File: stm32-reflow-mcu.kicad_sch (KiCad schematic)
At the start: 18 parts, among them J1 TC2030, J2 Conn_01x04_Male, J3 Conn_01x03_Male, J4 Screw_Terminal_01x02, J5 Screw_Terminal_01x02, U1 STM32F051R4Tx, U2 MAX31855KASA, U3 MAX31855KASA

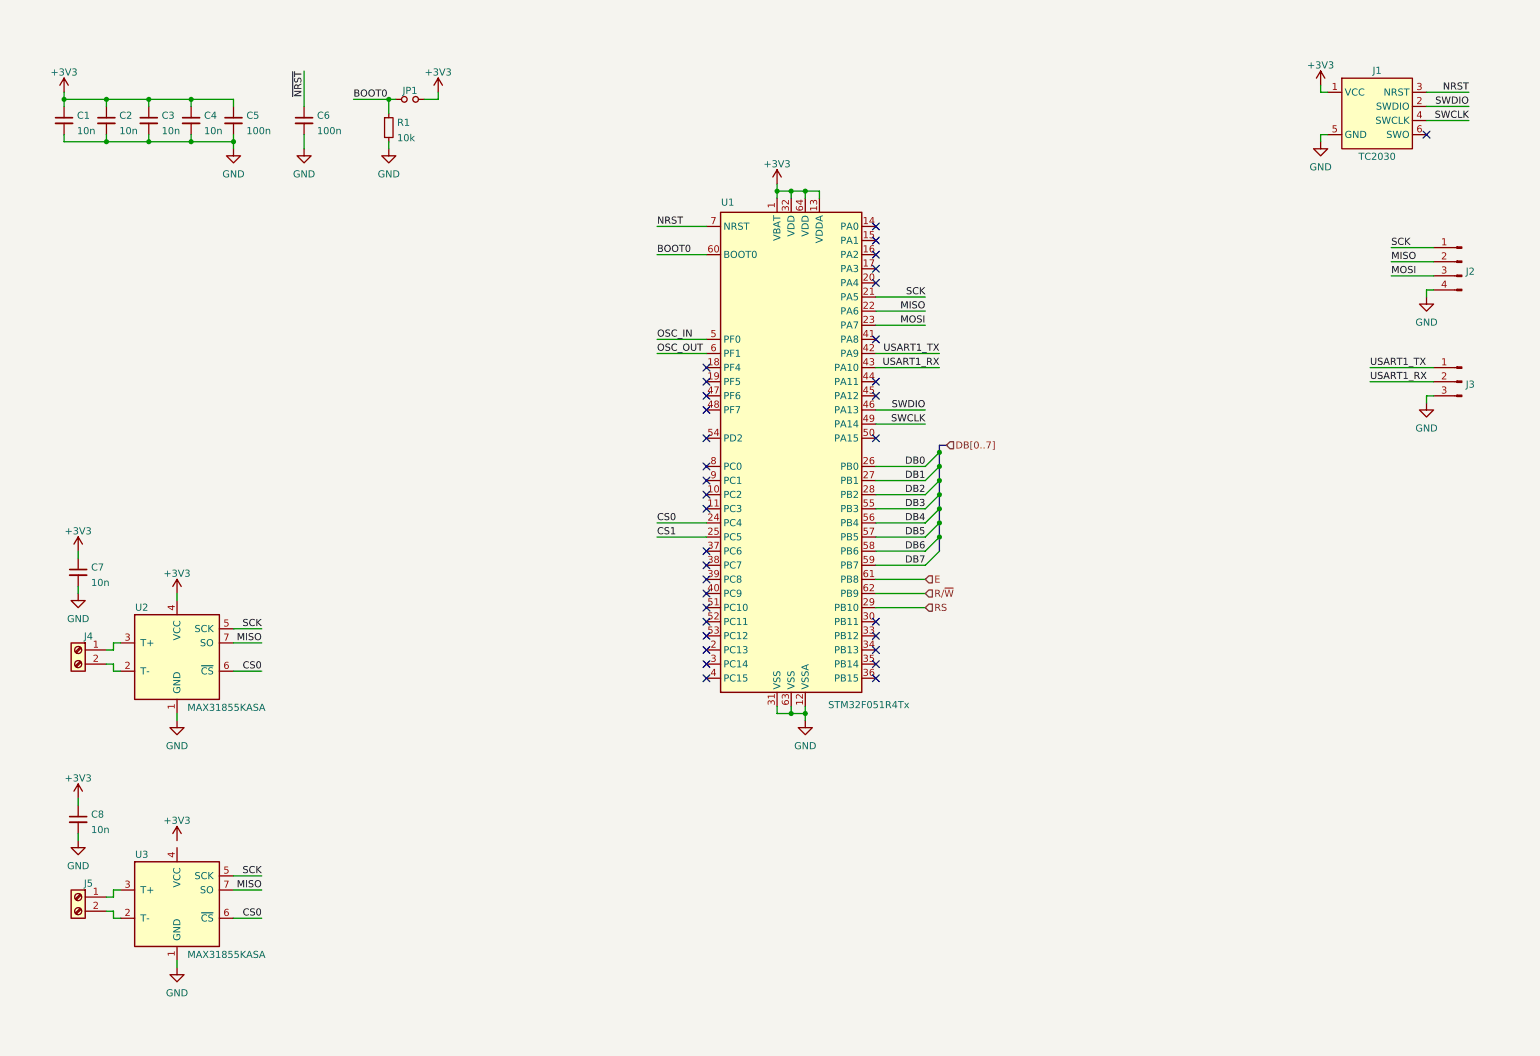
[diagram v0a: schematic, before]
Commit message: initial routing, added power supply source
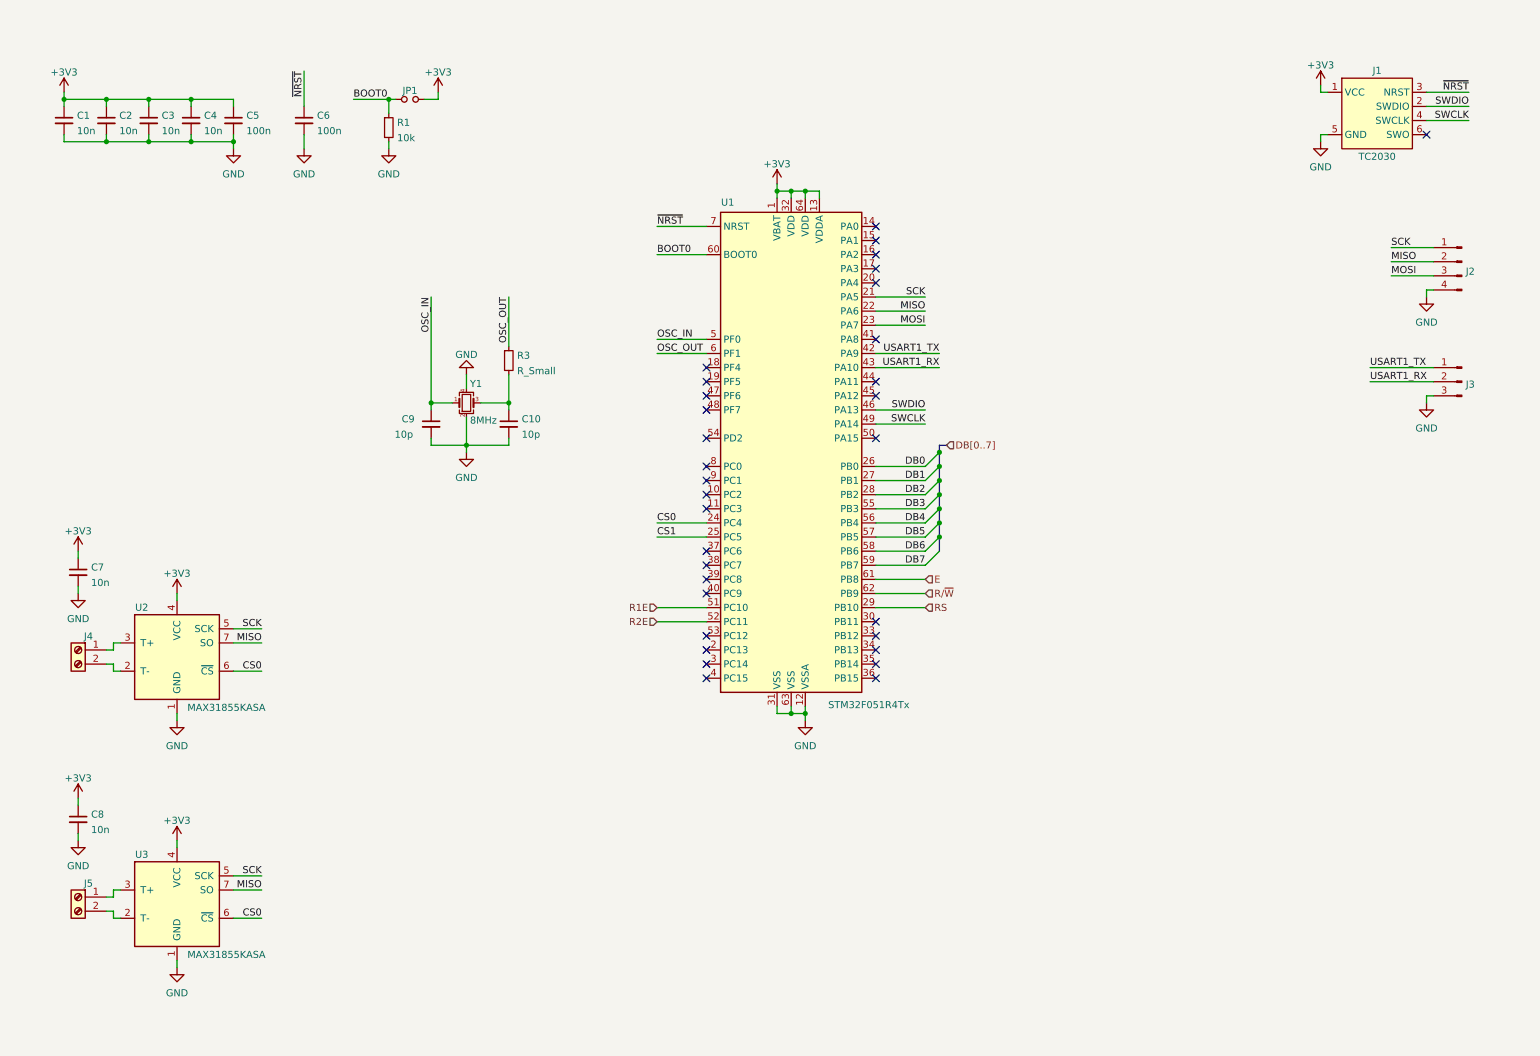
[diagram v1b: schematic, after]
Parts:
- added C10, C9: 10p, Capacitor_SMD:C_0603_1608Metric, symbol Device:C_Small
- added R3: R_Small, Resistor_SMD:R_0603_1608Metric, symbol Device:R_Small
- added Y1: 8MHz, Crystal:Crystal_SMD_5032-4Pin_5.0x3.2mm, symbol Device:Crystal_GND24_Small
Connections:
- net NRST is gone; now on net ~{NRST}: J1.3 (NRST), U1.7 (NRST)
- net +3V3: now also U3.4 (VCC)
- net GND: now also C10.2, C9.2, Y1.2, Y1.4
- net OSC_IN: now also C9.1, Y1.1
- net OSC_OUT: now also R3.1
- net R1E: now reaches U1.51 (PC10)
- net R2E: now reaches U1.52 (PC11)
- new net: C10.1, R3.2, Y1.3
- no-connect marks 34 -> 32
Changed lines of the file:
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@@
   (junction (at 52.07 35.56) (diameter 0) (color 0 0 0 0))
   (junction (at 80.01 27.94) (diameter 0) (color 0 0 0 0))
+  (junction (at 87.63 82.55) (diameter 0) (color 0 0 0 0))
+  (junction (at 93.98 90.17) (diameter 0) (color 0 0 0 0))
+  (junction (at 101.6 82.55) (diameter 0) (color 0 0 0 0))
   (junction (at 149.86 44.45) (diameter 0) (color 0 0 0 0))
   (junction (at 152.4 44.45) (diameter 0) (color 0 0 0 0))
@@
   (no_connect (at 137.16 114.3))
   (no_connect (at 137.16 116.84))
-  (no_connect (at 137.16 119.38))
-  (no_connect (at 137.16 121.92))
   (no_connect (at 137.16 124.46))
   (no_connect (at 137.16 127))
@@
     (stroke (width 0) (type default) (color 0 0 0 0))
   )
+  (wire (pts (xy 41.91 161.29) (xy 41.91 162.56))
+    (stroke (width 0) (type default) (color 0 0 0 0))
+  )
   (wire (pts (xy 41.91 182.88) (xy 41.91 184.15))
     (stroke (width 0) (type default) (color 0 0 0 0))
@@
     (stroke (width 0) (type default) (color 0 0 0 0))
   )
+  (wire (pts (xy 87.63 63.5) (xy 87.63 82.55))
+    (stroke (width 0) (type default) (color 0 0 0 0))
+  )
+  (wire (pts (xy 87.63 82.55) (xy 91.44 82.55))
+    (stroke (width 0) (type default) (color 0 0 0 0))
+  )
+  (wire (pts (xy 87.63 83.82) (xy 87.63 82.55))
+    (stroke (width 0) (type default) (color 0 0 0 0))
+  )
+  (wire (pts (xy 87.63 88.9) (xy 87.63 90.17))
+    (stroke (width 0) (type default) (color 0 0 0 0))
+  )
+  (wire (pts (xy 87.63 90.17) (xy 93.98 90.17))
+    (stroke (width 0) (type default) (color 0 0 0 0))
+  )
   (wire (pts (xy 88.9 27.94) (xy 88.9 26.67))
     (stroke (width 0) (type default) (color 0 0 0 0))
   )
+  (wire (pts (xy 93.98 77.47) (xy 93.98 80.01))
+    (stroke (width 0) (type default) (color 0 0 0 0))
+  )
+  (wire (pts (xy 93.98 85.09) (xy 93.98 90.17))
+    (stroke (width 0) (type default) (color 0 0 0 0))
+  )
+  (wire (pts (xy 93.98 90.17) (xy 93.98 91.44))
+    (stroke (width 0) (type default) (color 0 0 0 0))
+  )
+  (wire (pts (xy 93.98 90.17) (xy 101.6 90.17))
+    (stroke (width 0) (type default) (color 0 0 0 0))
+  )
+  (wire (pts (xy 96.52 82.55) (xy 101.6 82.55))
+    (stroke (width 0) (type default) (color 0 0 0 0))
+  )
+  (wire (pts (xy 101.6 63.5) (xy 101.6 72.39))
+    (stroke (width 0) (type default) (color 0 0 0 0))
+  )
+  (wire (pts (xy 101.6 77.47) (xy 101.6 82.55))
+    (stroke (width 0) (type default) (color 0 0 0 0))
+  )
+  (wire (pts (xy 101.6 82.55) (xy 101.6 83.82))
+    (stroke (width 0) (type default) (color 0 0 0 0))
+  )
+  (wire (pts (xy 101.6 88.9) (xy 101.6 90.17))
+    (stroke (width 0) (type default) (color 0 0 0 0))
+  )
   (wire (pts (xy 128.27 50.8) (xy 137.16 50.8))
     (stroke (width 0) (type default) (color 0 0 0 0))
@@
   )
   (wire (pts (xy 128.27 73.66) (xy 137.16 73.66))
+    (stroke (width 0) (type default) (color 0 0 0 0))
+  )
+  (wire (pts (xy 128.27 119.38) (xy 137.16 119.38))
+    (stroke (width 0) (type default) (color 0 0 0 0))
+  )
+  (wire (pts (xy 128.27 121.92) (xy 137.16 121.92))
     (stroke (width 0) (type default) (color 0 0 0 0))
   )
@@
     (effects (font (size 1.27 1.27)) (justify left bottom))
   )
-  (label "NRST" (at 128.27 50.8 0)
+  (label "OSC_IN" (at 87.63 63.5 270)
+    (effects (font (size 1.27 1.27)) (justify right bottom))
+  )
+  (label "OSC_OUT" (at 101.6 63.5 270)
+    (effects (font (size 1.27 1.27)) (justify right bottom))
+  )
+  (label "~{NRST}" (at 128.27 50.8 0)
     (effects (font (size 1.27 1.27)) (justify left bottom))
   )
@@
     (effects (font (size 1.27 1.27)) (justify left bottom))
   )
-  (label "NRST" (at 274.32 26.67 180)
+  (label "~{NRST}" (at 274.32 26.67 180)
     (effects (font (size 1.27 1.27)) (justify right bottom))
   )
@@
   (label "SWCLK" (at 274.32 31.75 180)
     (effects (font (size 1.27 1.27)) (justify right bottom))
+  )
+  (hierarchical_label "R1E" (shape input) (at 128.27 119.38 180)
+    (effects (font (size 1.27 1.27)) (justify right))
+  )
+  (hierarchical_label "R2E" (shape input) (at 128.27 121.92 180)
+    (effects (font (size 1.27 1.27)) (justify right))
   )
   (hierarchical_label "E" (shape input) (at 176.53 114.3 0)
@@
     (pin "1")
   )
+  (symbol (lib_id "power:GND") (at 93.98 77.47 180) (unit 1)
+    (in_bom yes) (on_board yes) (fields_autoplaced)
+    (property "Reference" "#PWR0102" (id 0) (at 93.98 71.12 0)
+      (effects (font (size 1.27 1.27)) hide)
+    )
+    (property "Value" "GND" (id 1) (at 93.98 73.8655 0))
+    (property "Footprint" "" (id 2) (at 93.98 77.47 0)
+      (effects (font (size 1.27 1.27)) hide)
+    )
+    (property "Datasheet" "" (id 3) (at 93.98 77.47 0)
+      (effects (font (size 1.27 1.27)) hide)
+    )
+    (pin "1")
+  )
+  (symbol (lib_id "power:GND") (at 93.98 91.44 0) (unit 1)
+    (in_bom yes) (on_board yes) (fields_autoplaced)
+    (property "Reference" "#PWR0101" (id 0) (at 93.98 97.79 0)
+      (effects (font (size 1.27 1.27)) hide)
+    )
+    (property "Value" "GND" (id 1) (at 93.98 96.0024 0))
+    (property "Footprint" "" (id 2) (at 93.98 91.44 0)
+      (effects (font (size 1.27 1.27)) hide)
+    )
+    (property "Datasheet" "" (id 3) (at 93.98 91.44 0)
+      (effects (font (size 1.27 1.27)) hide)
+    )
+    (pin "1")
+  )
   (symbol (lib_id "power:GND") (at 154.94 139.7 0) (unit 1)
     (in_bom yes) (on_board yes) (fields_autoplaced)
@@
     (pin "2")
   )
+  (symbol (lib_id "Device:R_Small") (at 101.6 74.93 0) (unit 1)
+    (in_bom yes) (on_board yes) (fields_autoplaced)
+    (property "Reference" "R3" (id 0) (at 103.0986 74.0215 0)
+      (effects (font (size 1.27 1.27)) (justify left))
+    )
+    (property "Value" "R_Small" (id 1) (at 103.0986 76.7966 0)
+      (effects (font (size 1.27 1.27)) (justify left))
+    )
+    (property "Footprint" "Resistor_SMD:R_0603_1608Metric" (id 2) (at 101.6 74.93 0)
+      (effects (font (size 1.27 1.27)) hide)
+    )
+    (property "Datasheet" "~" (id 3) (at 101.6 74.93 0)
+      (effects (font (size 1.27 1.27)) hide)
+    )
+    (pin "1")
+    (pin "2")
+  )
   (symbol (lib_id "Device:C_Small") (at 21.59 31.75 0) (unit 1)
     (in_bom yes) (on_board yes) (fields_autoplaced)
@@
     (pin "2")
   )
+  (symbol (lib_id "Device:C_Small") (at 87.63 86.36 0) (unit 1)
+    (in_bom yes) (on_board yes)
+    (property "Reference" "C9" (id 0) (at 82.3341 85.4515 0)
+      (effects (font (size 1.27 1.27)) (justify left))
+    )
+    (property "Value" "10p" (id 1) (at 81.0641 88.2266 0)
+      (effects (font (size 1.27 1.27)) (justify left))
+    )
+    (property "Footprint" "Capacitor_SMD:C_0603_1608Metric" (id 2) (at 87.63 86.36 0)
+      (effects (font (size 1.27 1.27)) hide)
+    )
+    (property "Datasheet" "~" (id 3) (at 87.63 86.36 0)
+      (effects (font (size 1.27 1.27)) hide)
+    )
+    (pin "1")
+    (pin "2")
+  )
+  (symbol (lib_id "Device:C_Small") (at 101.6 86.36 0) (unit 1)
+    (in_bom yes) (on_board yes) (fields_autoplaced)
+    (property "Reference" "C10" (id 0) (at 103.9241 85.4515 0)
+      (effects (font (size 1.27 1.27)) (justify left))
+    )
+    (property "Value" "10p" (id 1) (at 103.9241 88.2266 0)
+      (effects (font (size 1.27 1.27)) (justify left))
+    )
+    (property "Footprint" "Capacitor_SMD:C_0603_1608Metric" (id 2) (at 101.6 86.36 0)
+      (effects (font (size 1.27 1.27)) hide)
+    )
+    (property "Datasheet" "~" (id 3) (at 101.6 86.36 0)
+      (effects (font (size 1.27 1.27)) hide)
+    )
+    (pin "1")
+    (pin "2")
+  )
+  (symbol (lib_id "Device:Crystal_GND24_Small") (at 93.98 82.55 0) (unit 1)
+    (in_bom yes) (on_board yes)
+    (property "Reference" "Y1" (id 0) (at 94.6151 79.1015 0)
+      (effects (font (size 1.27 1.27)) (justify left))
+    )
+    (property "Value" "8MHz" (id 1) (at 94.6151 85.6866 0)
+      (effects (font (size 1.27 1.27)) (justify left))
+    )
+    (property "Footprint" "Crystal:Crystal_SMD_5032-4Pin_5.0x3.2mm" (id 2) (at 93.98 82.55 0)
+      (effects (font (size 1.27 1.27)) hide)
+    )
+    (property "Datasheet" "~" (id 3) (at 93.98 82.55 0)
+      (effects (font (size 1.27 1.27)) hide)
+    )
+    (pin "1")
+    (pin "2")
+    (pin "3")
+    (pin "4")
+  )
   (symbol (lib_id "Connector:Conn_01x03_Male") (at 273.05 78.74 0) (mirror y) (unit 1)

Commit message: finalized routing and circuit schematic (so far)
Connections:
- net CS0: no longer U3.6 (~{CS})
- net CS1: now also U3.6 (~{CS})
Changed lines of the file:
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@@
     (effects (font (size 1.27 1.27)) (justify right bottom))
   )
-  (label "CS0" (at 57.15 175.26 180)
+  (label "CS1" (at 57.15 175.26 180)
     (effects (font (size 1.27 1.27)) (justify right bottom))
   )

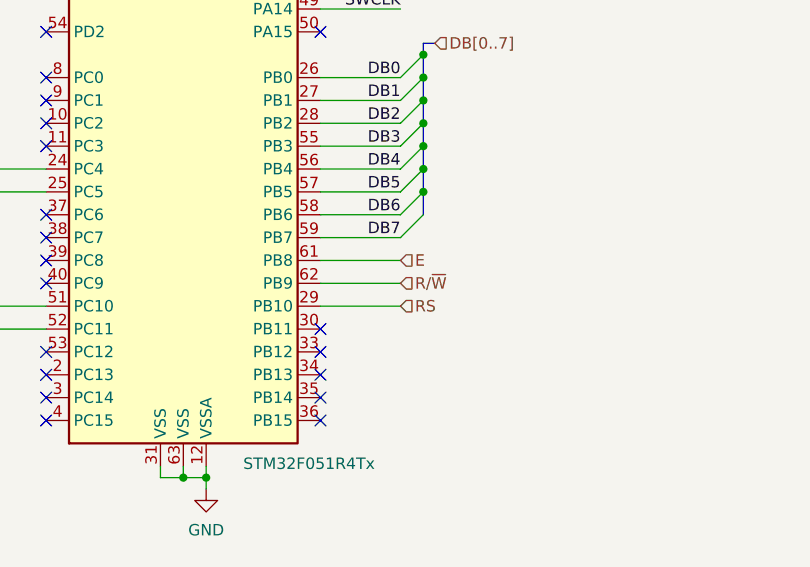
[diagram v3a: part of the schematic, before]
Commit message: downsized resistor network to 10
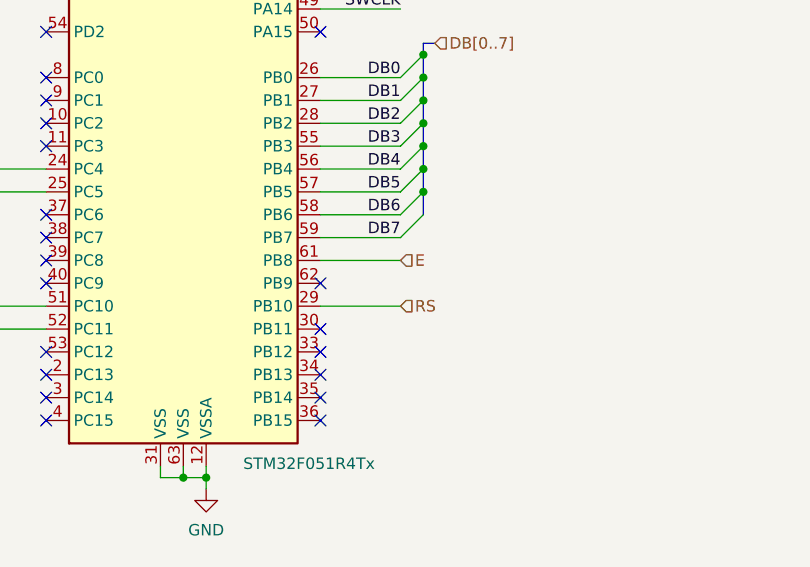
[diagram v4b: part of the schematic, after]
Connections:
- net R/~{W}: no longer names the net of U1.62 (PB9)
- no-connect marks 32 -> 33
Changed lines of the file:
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@@
   (no_connect (at 167.64 81.28))
   (no_connect (at 167.64 88.9))
+  (no_connect (at 167.64 116.84))
   (no_connect (at 167.64 121.92))
   (no_connect (at 167.64 124.46))
@@
     (stroke (width 0) (type default) (color 0 0 0 0))
   )
-  (wire (pts (xy 167.64 116.84) (xy 176.53 116.84))
-    (stroke (width 0) (type default) (color 0 0 0 0))
-  )
   (wire (pts (xy 167.64 119.38) (xy 176.53 119.38))
     (stroke (width 0) (type default) (color 0 0 0 0))
@@
     (effects (font (size 1.27 1.27)) (justify left))
   )
-  (hierarchical_label "R{slash}~{W}" (shape input) (at 176.53 116.84 0)
-    (effects (font (size 1.27 1.27)) (justify left))
-  )
